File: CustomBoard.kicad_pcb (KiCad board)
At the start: 4 copper layers, 40.9 x 34.1 mm, 36 parts, among them J1 RIGHT, J10 Sensor08, J11 Sensor09, J12 Sensor10, J13 Sensor11, J14 Sensor12, J2 LEFT, J3 Sensor01, J4 Sensor02, J5 Sensor03, J6 Sensor04, J7 Sensor05, J8 Sensor06, J9 Sensor07, U1 DS28E05, U2 PCA9555, U3 VL53L1X

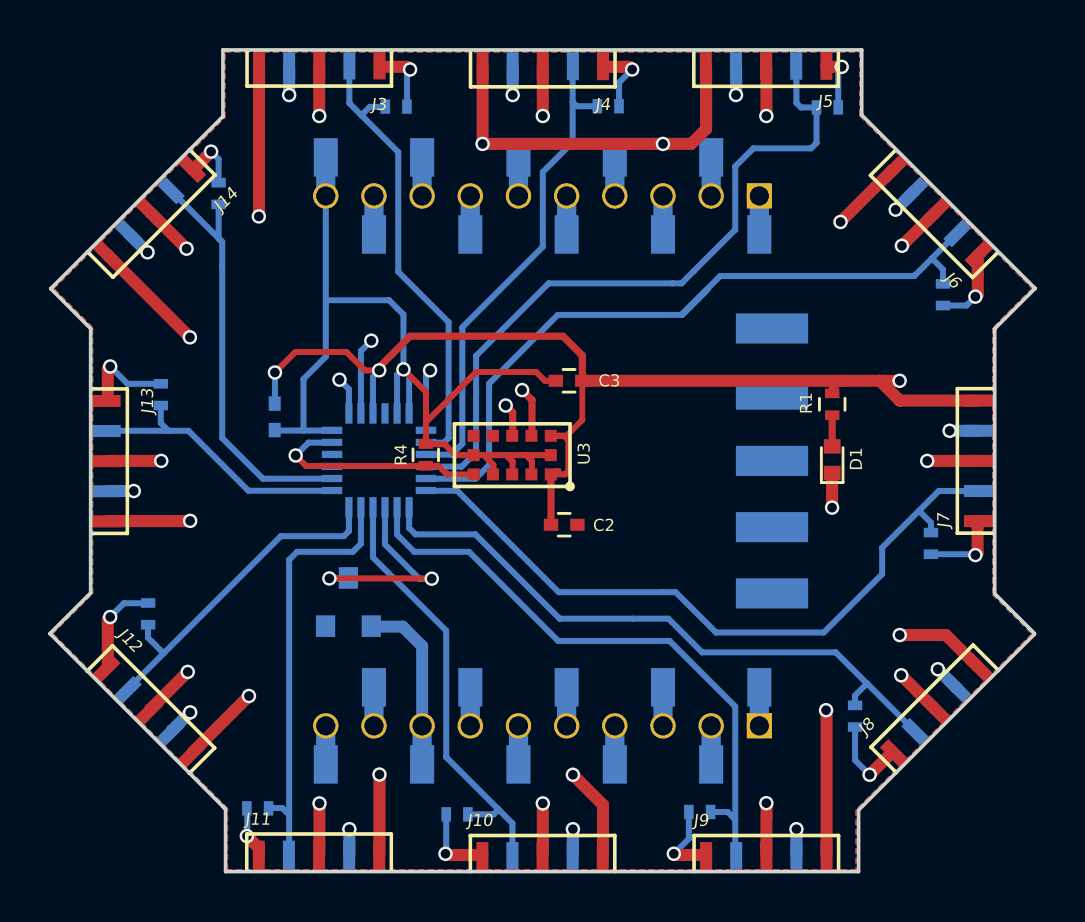
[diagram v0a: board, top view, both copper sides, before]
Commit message: integrate cam module in main board
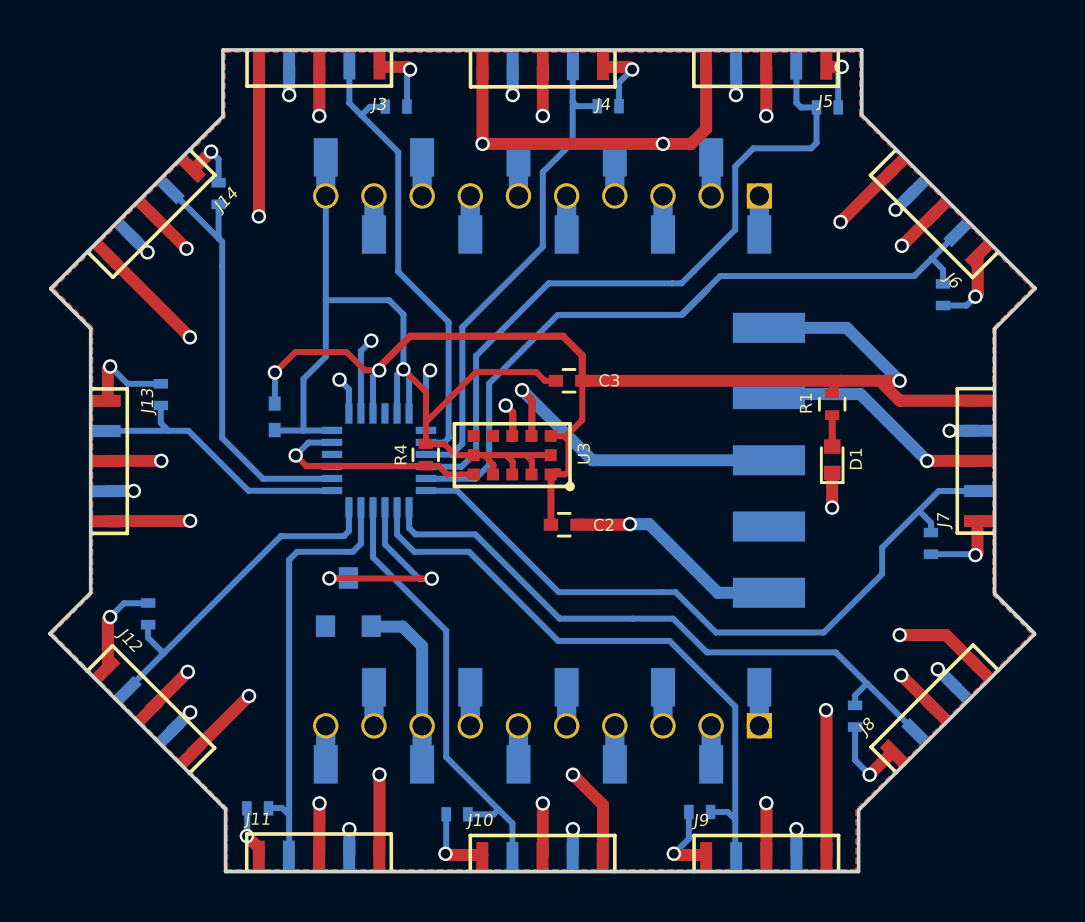
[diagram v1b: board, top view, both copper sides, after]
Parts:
- removed REF**: AMGCam, footprint:AMGCam
- added J15: Camera, footprint:AMGCam, B.Cu at (148.4, 97.0)
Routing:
- net SCL: track 161.9 -> 173.4 mm
- net GND: track 214.5 -> 223.6 mm, vias 15 -> 16
- net SDA: track 160.5 -> 168.2 mm
- net VCC: track 194.5 -> 200.8 mm
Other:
- board text added: "Camera GND"
- board text added: "Camera VCC"
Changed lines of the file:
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@@
 (kicad_pcb (version 4) (host pcbnew 4.0.7-e2-6376~58~ubuntu16.04.1)
   (general
-    (links 155)
+    (links 159)
     (no_connects 0)
     (area 118.474999 79.864999 159.525001 114.125001)
     (thickness 0.8)
-    (drawings 18023)
-    (tracks 554)
+    (drawings 18025)
+    (tracks 566)
     (zones 0)
     (modules 36)
@@
   )
   (setup
-    (last_trace_width 0.25)
+    (last_trace_width 0.5)
     (user_trace_width 0.3)
     (user_trace_width 0.5)
@@
   )
   (module footprint:AMGCam (layer B.Cu)
-    (at 148.525 97 270)
-    (fp_text reference REF** (at -5.8 2.7 270) (layer B.SilkS)
+    (at 148.4 96.975 90)
+    (fp_text reference J15 (at -5.8 2.7 90) (layer B.SilkS)
       (effects (font (size 0.5 0.5) (thickness 0.1)) (justify mirror))
     )
-    (fp_text value AMGCam (at 0 2.7 270) (layer B.Fab)
+    (fp_text value Camera (at 0 2.7 90) (layer B.Fab)
       (effects (font (size 0.5 0.5) (thickness 0.1)) (justify mirror))
     )
@@
     (fp_line (start -6.6 2) (end -6.7 2) (layer B.SilkS) (width 0.15))
     (fp_line (start -6.7 2) (end -6.7 -1.5) (layer B.SilkS) (width 0.15))
-    (pad 1 smd rect (at -5.5 0 270) (size 1.25 3) (layers B.Cu B.Paste B.Mask))
-    (pad 2 smd rect (at -2.75 0 270) (size 1.25 3) (layers B.Cu B.Paste B.Mask))
-    (pad 3 smd rect (at 0 0 270) (size 1.25 3) (layers B.Cu B.Paste B.Mask))
-    (pad 4 smd rect (at 2.75 0 270) (size 1.25 3) (layers B.Cu B.Paste B.Mask))
-    (pad 5 smd rect (at 5.5 0 270) (size 1.25 3) (layers B.Cu B.Paste B.Mask))
+    (pad 1 smd rect (at -5.5 0 90) (size 1.25 3) (layers B.Cu B.Paste B.Mask)
+      (net 1 GND))
+    (pad 2 smd rect (at -2.75 0 90) (size 1.25 3) (layers B.Cu B.Paste B.Mask))
+    (pad 3 smd rect (at 0 0 90) (size 1.25 3) (layers B.Cu B.Paste B.Mask)
+      (net 6 SCL))
+    (pad 4 smd rect (at 2.75 0 90) (size 1.25 3) (layers B.Cu B.Paste B.Mask)
+      (net 5 SDA))
+    (pad 5 smd rect (at 5.5 0 90) (size 1.25 3) (layers B.Cu B.Paste B.Mask)
+      (net 2 VCC))
+  )
+  (gr_text "Camera\nVCC" (at 145 91.425) (layer B.SilkS)
+    (effects (font (size 0.5 0.5) (thickness 0.1)) (justify mirror))
+  )
+  (gr_text "Camera\nGND" (at 145.075 102.45) (layer B.SilkS)
+    (effects (font (size 0.5 0.5) (thickness 0.1)) (justify mirror))
   )
   (gr_line (start 125.84 111.46) (end 125.75 111.37) (angle 90) (layer Edge.Cuts) (width 0.15))
@@
   (gr_line (start 183.551 150.189) (end 175.849 152.992) (layer Eco1.User) (width 0.1))
   (gr_line (start 189.83 144.921) (end 183.551 150.189) (layer Eco1.User) (width 0.1))
+  (segment (start 148.4 102.475) (end 146.275 102.475) (width 0.5) (layer B.Cu) (net 1))
+  (segment (start 142.6 99.65) (end 140.45 99.65) (width 0.5) (layer F.Cu) (net 1))
+  (segment (start 142.625 99.625) (end 142.6 99.65) (width 0.5) (layer F.Cu) (net 1))
+  (via (at 142.625 99.625) (size 0.6) (drill 0.4) (layers F.Cu B.Cu) (net 1))
+  (segment (start 143.425 99.625) (end 142.625 99.625) (width 0.5) (layer B.Cu) (net 1))
+  (segment (start 146.275 102.475) (end 143.425 99.625) (width 0.5) (layer B.Cu) (net 1))
   (segment (start 130 84.4) (end 130 86) (width 0.8) (layer B.Cu) (net 1))
   (segment (start 139.55 93.675) (end 139.1 93.675) (width 0.25) (layer F.Cu) (net 1))
@@
   (segment (start 133.075 93.3) (end 132.96 93.415) (width 0.25) (layer B.Cu) (net 1))
   (segment (start 130 84.825) (end 130 90.33) (width 0.25) (layer B.Cu) (net 1))
+  (segment (start 148.4 91.475) (end 151.625 91.475) (width 0.5) (layer B.Cu) (net 2))
+  (segment (start 151.625 91.475) (end 153.825 93.675) (width 0.5) (layer B.Cu) (net 2))
   (segment (start 152.95 93.675) (end 153.825 93.675) (width 0.5) (layer F.Cu) (net 2))
   (segment (start 153.825 93.675) (end 153.85 93.675) (width 0.5) (layer B.Cu) (net 2))
@@
   (segment (start 134.16 93.41) (end 134.33 93.24) (width 0.25) (layer B.Cu) (net 4))
   (segment (start 134.16 95.74) (end 134.16 93.41) (width 0.25) (layer B.Cu) (net 4))
+  (segment (start 148.4 94.225) (end 152.195 94.225) (width 0.5) (layer B.Cu) (net 5))
+  (segment (start 152.195 94.225) (end 154.97 97) (width 0.5) (layer B.Cu) (net 5))
   (segment (start 142 86) (end 142 84.4) (width 0.8) (layer B.Cu) (net 5))
   (segment (start 131.89 92.01) (end 134.78 92.01) (width 0.5) (layer B.SDA) (net 5))
@@
   (segment (start 142.32 82.68) (end 148.29 82.68) (width 0.5) (layer B.SDA) (net 5))
   (via (at 129.74 111.22) (size 0.6) (drill 0.4) (layers F.Cu B.Cu) (net 5))
+  (segment (start 148.4 96.975) (end 141.065 96.975) (width 0.5) (layer B.Cu) (net 6))
+  (segment (start 141.065 96.975) (end 138.15 94.06) (width 0.5) (layer B.Cu) (net 6))
   (segment (start 140 86) (end 140 87.6) (width 0.8) (layer B.Cu) (net 6))
   (segment (start 138.15 94.06) (end 138.15 93.27) (width 0.5) (layer A.SCL) (net 6))
@@
   (segment (start 134.15 96.74) (end 135.22 96.74) (width 0.25) (layer B.Cu) (net 8))
   (segment (start 140.25 82.1) (end 140.25 80.64) (width 0.25) (layer B.Cu) (net 8))
-  (segment (start 150.375 82.325) (end 150.375 83.8) (width 0.25) (layer B.Cu) (net 9) (status 400000))
+  (segment (start 150.375 82.325) (end 150.375 83.8) (width 0.25) (layer B.Cu) (net 9))
   (segment (start 147 87.4) (end 145.275 89.125) (width 0.25) (layer B.Cu) (net 9))
   (segment (start 147 84.775) (end 147 87.4) (width 0.25) (layer B.Cu) (net 9))
@@
   (segment (start 135.46 98.24) (end 139.67 102.45) (width 0.25) (layer B.Cu) (net 11))
   (segment (start 134.17 98.25) (end 134.16 98.24) (width 0.25) (layer B.Cu) (net 11))
-  (segment (start 142.75 103.55) (end 144.225 103.55) (width 0.25) (layer B.Cu) (net 12))
+  (segment (start 142.75 103.55) (end 144.425 103.55) (width 0.25) (layer B.Cu) (net 12))
   (segment (start 151.175 104.95) (end 152.4675 106.2425) (width 0.25) (layer B.Cu) (net 12))
-  (segment (start 145.625 104.95) (end 151.175 104.95) (width 0.25) (layer B.Cu) (net 12))
-  (segment (start 144.225 103.55) (end 145.625 104.95) (width 0.25) (layer B.Cu) (net 12))
+  (segment (start 145.825 104.95) (end 151.175 104.95) (width 0.25) (layer B.Cu) (net 12))
+  (segment (start 144.425 103.55) (end 145.825 104.95) (width 0.25) (layer B.Cu) (net 12))
   (segment (start 151.975 107.15) (end 151.975 106.735) (width 0.25) (layer B.Cu) (net 12))
   (segment (start 151.975 106.735) (end 152.4675 106.2425) (width 0.25) (layer B.Cu) (net 12))

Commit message: reformatting
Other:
- board text added: "1"
- board text added: "2"
- board text added: "3"
- board text added: "Obstacle Avoidance Deck"
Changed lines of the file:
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@@
     (area 118.474999 79.864999 159.525001 114.125001)
     (thickness 0.8)
-    (drawings 18025)
+    (drawings 18029)
     (tracks 566)
     (zones 0)
@@
   )
   (setup
-    (last_trace_width 0.5)
+    (last_trace_width 0.25)
     (user_trace_width 0.3)
     (user_trace_width 0.5)
@@
       (padsonsilk false)
       (subtractmaskfromsilk false)
-      (outputformat 4)
+      (outputformat 1)
       (mirror false)
       (drillshape 0)
       (scaleselection 1)
-      (outputdirectory pdfs/))
+      (outputdirectory gerbers/))
   )
   (net 0 "")
@@
   (module footprint:AMGCam (layer B.Cu)
     (at 148.4 96.975 90)
-    (fp_text reference J15 (at -5.8 2.7 90) (layer B.SilkS)
+    (fp_text reference J15 (at 0.05 -2.45 90) (layer B.SilkS)
       (effects (font (size 0.5 0.5) (thickness 0.1)) (justify mirror))
     )
@@
       (net 2 VCC))
   )
+  (gr_text 3 (at 144.725 80.65) (layer B.SilkS)
+    (effects (font (size 0.5 0.5) (thickness 0.125)) (justify mirror))
+  )
+  (gr_text 2 (at 135.425 80.625) (layer B.SilkS)
+    (effects (font (size 0.5 0.5) (thickness 0.125)) (justify mirror))
+  )
+  (gr_text 1 (at 126.225 80.7) (layer B.SilkS)
+    (effects (font (size 0.5 0.5) (thickness 0.125)) (justify mirror))
+  )
+  (gr_text "Obstacle\nAvoidance\nDeck" (at 138.775 97.075 90) (layer B.SilkS)
+    (effects (font (size 1 1) (thickness 0.25)) (justify mirror))
+  )
   (gr_text "Camera\nVCC" (at 145 91.425) (layer B.SilkS)
